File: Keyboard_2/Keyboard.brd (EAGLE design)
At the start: 479.1 x 340.4 mm, 762 parts, among them IC1 MEGA8-AI, J1 J, J10 J, J11 J, J12 J, J13 J, J14 J, J15 J, J16 J, J17 J, J2 J, J3 J, J4 J, J5 J, J6 J, J7 J, J8 J, J9 J

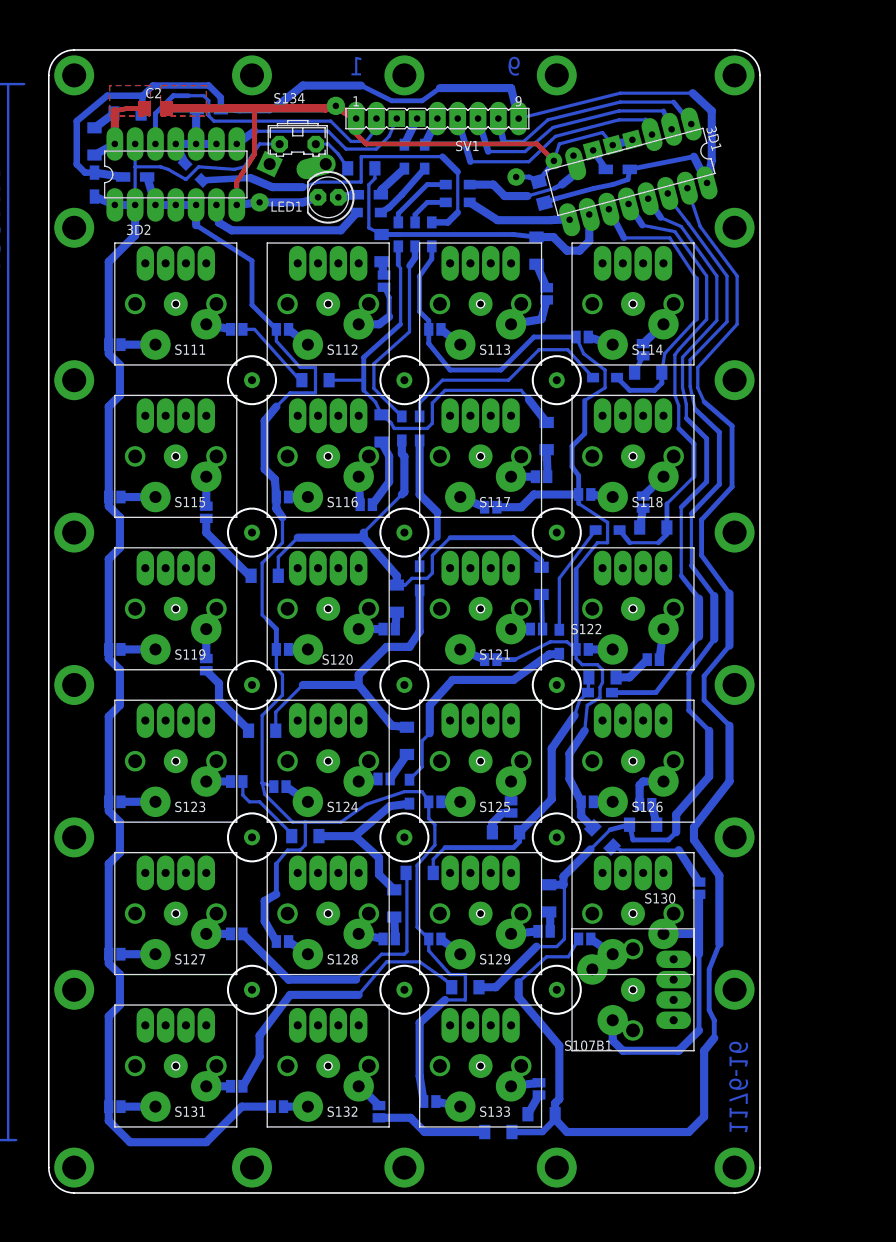
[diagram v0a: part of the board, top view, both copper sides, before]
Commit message: del 1 wire
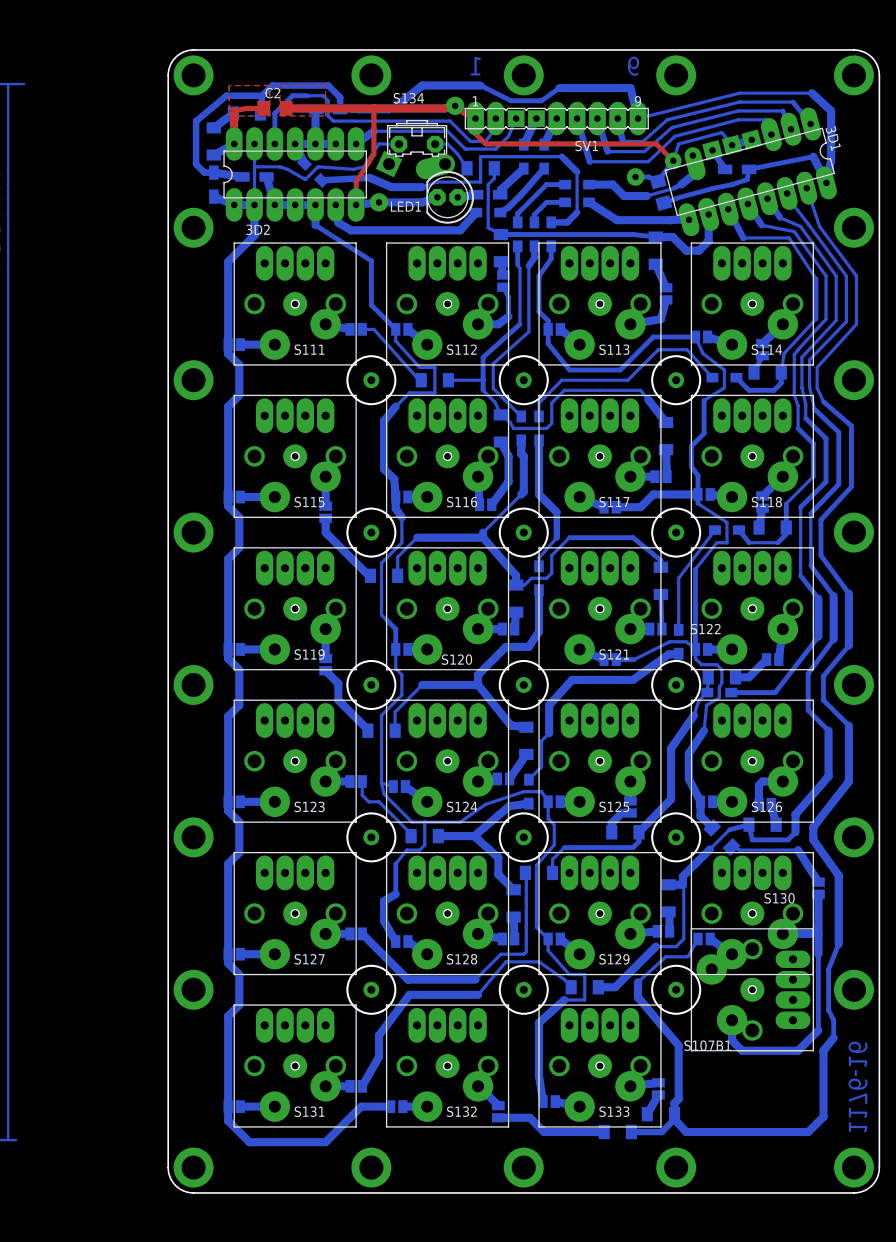
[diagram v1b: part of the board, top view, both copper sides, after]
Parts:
- moved 3D1 14.9 mm to (478.5, 134.6)
- moved 3D2 14.9 mm to (421.6, 134.3)
- moved C1 14.9 mm to (467.4, 132.1)
- moved C2 14.9 mm to (419.1, 142.6)
- moved D111 14.9 mm to (439.1, 108.6)
- moved D112 14.9 mm to (444.8, 135.1)
- moved D113 14.9 mm to (447.4, 125.1)
- moved D114 14.9 mm to (466.7, 124.8)
- moved D115 14.9 mm to (480.7, 109.5)
- moved D116 14.9 mm to (432.8, 84.1)
- moved D117 14.9 mm to (447.4, 102.6)
- moved D118 14.9 mm to (468.0, 101.6)
- moved D120 14.9 mm to (432.4, 64.8)
- moved D121 14.9 mm to (449.3, 81.3)
- moved D122 14.9 mm to (467.4, 83.5)
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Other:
- board size 479.1 x 340.4 mm -> 494 x 340.4 mm
